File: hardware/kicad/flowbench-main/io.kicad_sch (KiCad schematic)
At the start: 57 parts, among them J18 Expander 2 spare, J19 Bleed stepper signals (GX16-8), J20 Bleed stepper 24 V (GX12-2), J21 Lift stepper signals (GX16-8), J22 Lift stepper 24 V (GX12-2), J23 Motor housing coils (GX16-8), J24 Motors-armed lamp, J25 E-stop (2 NC contacts), U11 TCA9535PWR #1 (0x20), U12 TCA9535PWR #2 (0x21), U13 TLP291-4, U14 TLP291-4, U15 TLP291-4, U16 AM26C31 (bleed stepper), U17 AM26C31 (lift stepper), U18 TBD62083AFWG, U19 74HCT123

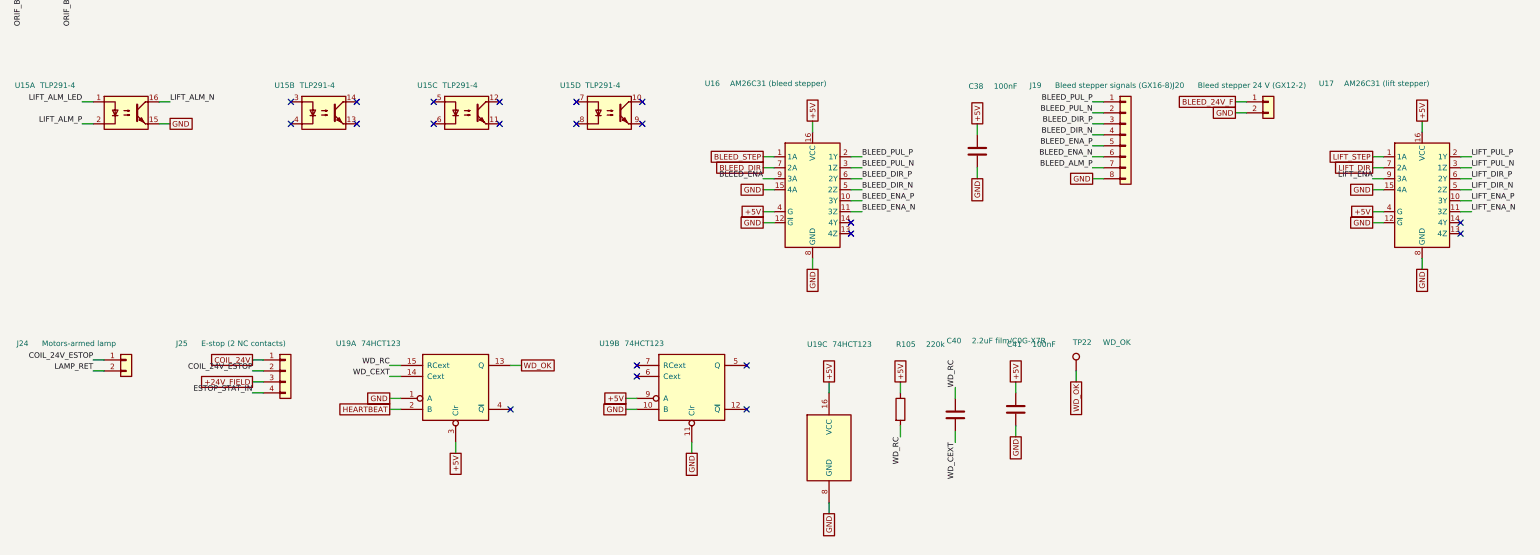
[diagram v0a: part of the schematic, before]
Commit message: KiCad: fix off-grid pins on ADS1219 and AM26C31 symbols
A floating-point modulo misread the symbol half-height as off-grid and
shifted it by half a step, leaving top and bottom pins 0.635 mm off the
1.27 mm connection grid (16 ERC warnings). verify.py now checks every pin
and wire end against the grid.

Co-Authored-By: Claude Opus 5.5 <noreply@anthropic.com>
Claude-Session: https://claude.ai/code/session_01QEmmugJA9S77dSDSNcKrPa
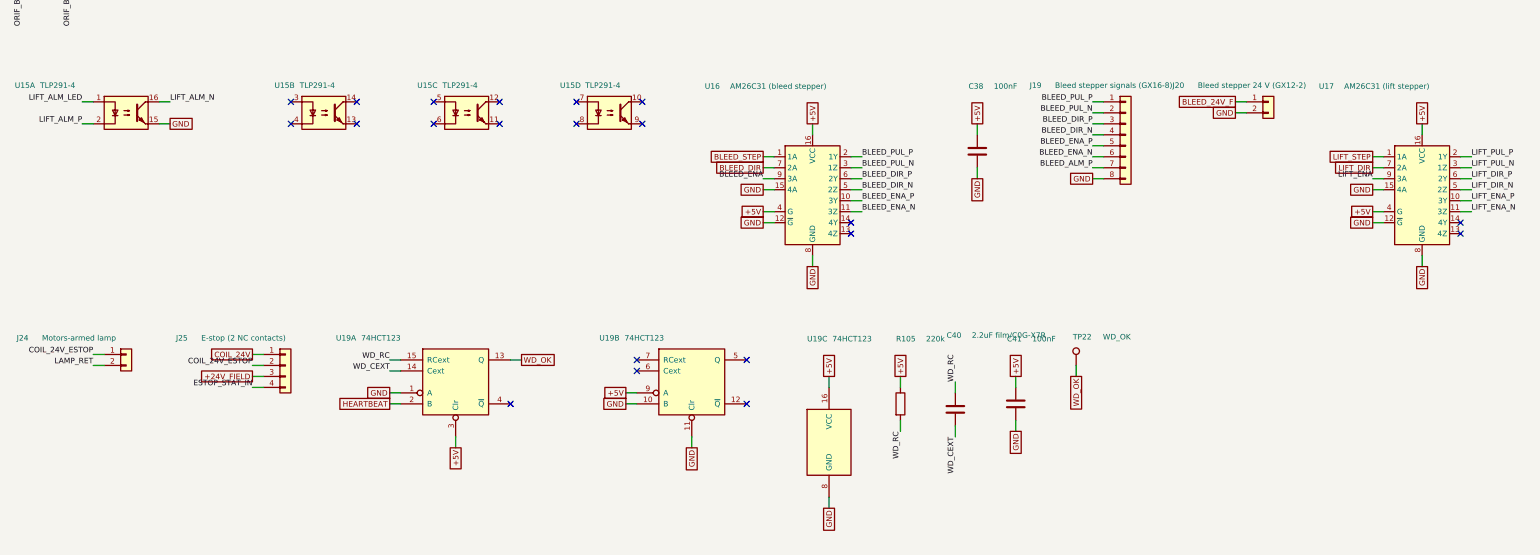
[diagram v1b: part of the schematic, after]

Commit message: KiCad: WIZ850io as one part with a two-row footprint
Pinout and size confirmed from the module (20 x 25 mm, two 1x6 headers).
The two header symbols become one 12-pin WIZ850io part on footprint
FlowBench:WIZ850io (J1 pads 1-6, J2 pads 7-12, rows 17.78 mm apart), so the
headers can't be placed at the wrong spacing.

Co-Authored-By: Claude Opus 5.5 <noreply@anthropic.com>
Claude-Session: https://claude.ai/code/session_01QEmmugJA9S77dSDSNcKrPa
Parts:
- removed J18: Expander 2 spare, Connector_PinHeader_2.54mm:PinHeader_1x10_P2.54mm_Vertical, symbol FlowBench:Conn_01x10
- removed J23: Motor housing coils (GX16-8), Connector_Phoenix_MC:PhoenixContact_MC_1,5_8-G-3.81_1x08_P3.81mm_Horizontal, symbol FlowBench:Conn_01x08
- removed J24: Motors-armed lamp, Connector_Phoenix_MC:PhoenixContact_MC_1,5_2-G-3.81_1x02_P3.81mm_Horizontal, symbol FlowBench:Conn_01x02
- removed J25: E-stop (2 NC contacts), Connector_Phoenix_MC:PhoenixContact_MC_1,5_4-G-3.81_1x04_P3.81mm_Horizontal, symbol FlowBench:Conn_01x04
- removed U11: TCA9535PWR #1 (0x20), Package_SO:TSSOP-24_4.4x7.8mm_P0.65mm, symbol FlowBench:TCA9535PWR
- removed U13: TLP291-4, Package_SO:SOIC-16_4.55x10.3mm_P1.27mm, symbol FlowBench:TLP291-4
- removed U16: AM26C31 (bleed stepper), Package_SO:SOIC-16_3.9x9.9mm_P1.27mm, symbol FlowBench:AM26C31
- removed U18: TBD62083AFWG, Package_SO:SOIC-18W_7.5x11.6mm_P1.27mm, symbol FlowBench:TBD62083AFWG
- removed U19: 74HCT123, Package_SO:SOIC-16_3.9x9.9mm_P1.27mm, symbol FlowBench:74HCT123
- added J16: Expander 2 spare, Connector_PinHeader_2.54mm:PinHeader_1x10_P2.54mm_Vertical, symbol FlowBench:Conn_01x10
- added J17: Bleed stepper signals (GX16-8), Connector_Phoenix_MC:PhoenixContact_MC_1,5_8-G-3.81_1x08_P3.81mm_Horizontal, symbol FlowBench:Conn_01x08
- added J18: Bleed stepper 24 V (GX12-2), Connector_Phoenix_MSTB:PhoenixContact_MSTBA_2,5_2-G-5,08_1x02_P5.08mm_Horizontal, symbol FlowBench:Conn_01x02
- added J23: E-stop (2 NC contacts), Connector_Phoenix_MC:PhoenixContact_MC_1,5_4-G-3.81_1x04_P3.81mm_Horizontal, symbol FlowBench:Conn_01x04
- added U13: TCA9535PWR #2 (0x21), Package_SO:TSSOP-24_4.4x7.8mm_P0.65mm, symbol FlowBench:TCA9535PWR
- added U16: TLP291-4, Package_SO:SOIC-16_4.55x10.3mm_P1.27mm, symbol FlowBench:TLP291-4
- added U18: AM26C31 (lift stepper), Package_SO:SOIC-16_3.9x9.9mm_P1.27mm, symbol FlowBench:AM26C31
- added U19: TBD62083AFWG, Package_SO:SOIC-18W_7.5x11.6mm_P1.27mm, symbol FlowBench:TBD62083AFWG
- added U20: 74HCT123, Package_SO:SOIC-16_3.9x9.9mm_P1.27mm, symbol FlowBench:74HCT123
- J19: value Bleed stepper signals (GX16-8) -> Lift stepper signals (GX16-8)
- J20: value Bleed stepper 24 V (GX12-2) -> Lift stepper 24 V (GX12-2)
- J21: value Lift stepper signals (GX16-8) -> Motor housing coils (GX16-8)
- J22: value Lift stepper 24 V (GX12-2) -> Motors-armed lamp; footprint Connector_Phoenix_MSTB:PhoenixContact_MSTBA_2,5_2-G-5,08_1x02_P5.08mm_Horizontal -> Connector_Phoenix_MC:PhoenixContact_MC_1,5_2-G-3.81_1x02_P3.81mm_Horizontal
- U12: value TCA9535PWR #2 (0x21) -> TCA9535PWR #1 (0x20)
- U17: value AM26C31 (lift stepper) -> AM26C31 (bleed stepper)
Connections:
- net +24V_FIELD: now also J23.3 (Pin_3)
- net +3V3: now also J16.9 (Pin_9), U13.21 (A0), U13.24 (VCC); no longer U12.21 (A0)
- net +5V: now also U18.16 (VCC), U18.4 (G), U20.16 (VCC), U20.3 (Clr), U20.9 (A)
- net BLEED_24V_F: now also J18.1 (Pin_1); no longer J20.1 (Pin_1)
- net BLEED_ALM_LED: now also U15.7; no longer U14.7
- net BLEED_ALM_N: now also U15.10, U13.9 (P05); no longer U12.9 (P05), U14.10
- net BLEED_ALM_P: now also U15.8, J17.7 (Pin_7); no longer J19.7 (Pin_7), U14.8
- net BLEED_DIR: now also U17.7 (2A)
- net BLEED_DIR_N: now also U17.5 (2Z), J17.4 (Pin_4); no longer J19.4 (Pin_4)
- net BLEED_DIR_P: now also U17.6 (2Y), J17.3 (Pin_3); no longer J19.3 (Pin_3)
- net BLEED_ENA: now also U12.13 (P10), U17.9 (3A)
- net BLEED_ENA_N: now also U17.11 (3Z), J17.6 (Pin_6); no longer J19.6 (Pin_6)
- net BLEED_ENA_P: now also U17.10 (3Y), J17.5 (Pin_5); no longer J19.5 (Pin_5)
- net BLEED_HOME_IN_LED: now also U14.3
- net BLEED_HOME_N: now also U12.16 (P13), U14.14
- net BLEED_PUL_N: now also U17.3 (1Z), J17.2 (Pin_2); no longer J19.2 (Pin_2)
- net BLEED_PUL_P: now also U17.2 (1Y), J17.1 (Pin_1); no longer J19.1 (Pin_1)
- net BLEED_PWR_EN: now also U12.11 (P07)
- net BLEED_STEP: now also U17.1 (1A)
- net COIL1_CMD: now also U12.4 (P00), U19.1 (I1)
- net COIL1_RET: now also J21.2 (Pin_2), U19.18 (O1)
- net COIL2_CMD: now also U12.5 (P01), U19.2 (I2)
- net COIL2_RET: now also J21.3 (Pin_3), U19.17 (O2)
- net COIL3_CMD: now also U12.6 (P02), U19.3 (I3)
- net COIL3_RET: now also J21.4 (Pin_4), U19.16 (O3)
- net COIL4_CMD: now also U12.7 (P03), U19.4 (I4)
- net COIL4_RET: now also J21.5 (Pin_5), U19.15 (O4)
- net COIL5_CMD: now also U12.8 (P04), U19.5 (I5)
- net COIL5_RET: now also J21.6 (Pin_6), U19.14 (O5)
- net COIL6_CMD: now also U12.9 (P05), U19.6 (I6)
- net COIL6_RET: now also J21.7 (Pin_7), U19.13 (O6)
- net COIL_24V: now also J23.1 (Pin_1)
- net COIL_24V_ESTOP: now also J21.1 (Pin_1), J22.1 (Pin_1), J23.2 (Pin_2), U19.10 (COM)
- net EFUSE_FLT_N: now also U13.11 (P07); no longer U12.11 (P07)
- net ESTOP_OK_N: now also U12.15 (P12), U14.16
- net ESTOP_STAT_IN: now also J23.4 (Pin_4)
- net ESTOP_STAT_IN_LED: now also U14.1
- net ETH_INT_EXP: now also U13.10 (P06); no longer U12.10 (P06)
- net ETH_RST_N: now also U12.14 (P11)
- net EXP2_P10: now also J16.1 (Pin_1), U13.13 (P10); no longer U12.13 (P10)
- net EXP2_P11: now also J16.2 (Pin_2), U13.14 (P11); no longer U12.14 (P11)
- net EXP2_P12: now also J16.3 (Pin_3), U13.15 (P12); no longer U12.15 (P12)
- net EXP2_P13: now also J16.4 (Pin_4), U13.16 (P13); no longer U12.16 (P13)
- net EXP2_P14: now also J16.5 (Pin_5), U13.17 (P14); no longer U12.17 (P14)
- net EXP2_P15: now also J16.6 (Pin_6), U13.18 (P15); no longer U12.18 (P15)
- net EXP2_P16: now also J16.7 (Pin_7), U13.19 (P16); no longer U12.19 (P16)
- net EXP2_P17: now also J16.8 (Pin_8), U13.20 (P17); no longer U12.20 (P17)
- net EXP_INT_N: now also U13.1 (~{INT})
- net GND: now also U12.21 (A0), U14.8, U15.11, U15.13, U15.2, U15.4, U15.6, U15.9, J16.10 (Pin_10), J17.8 (Pin_8), J18.2 (Pin_2), U13.12 (GND), U13.2 (A1), U13.3 (A2), U16.15, U18.12 (~{G}), U18.15 (4A), U18.8 (GND), U19.8 (I8), U19.9 (GND), U20.1 (A), U20.10 (B), U20.11 (Clr), U20.8 (GND); no longer J21.8 (Pin_8), J22.2 (Pin_2)
- net HEARTBEAT: now also U20.2 (B)
- net LAMP_CMD: now also U12.10 (P06), U19.7 (I7)
- net LAMP_RET: now also J22.2 (Pin_2), U19.12 (O7)
- net LIFT_24V_F: now also J20.1 (Pin_1); no longer J22.1 (Pin_1)
- net LIFT_ALM_LED: now also U16.1; no longer U15.1
- net LIFT_ALM_N: now also U13.6 (P02), U16.16; no longer U12.6 (P02), U15.16
- net LIFT_ALM_P: now also J19.7 (Pin_7), U16.2; no longer J21.7 (Pin_7), U15.2
- net LIFT_DIR: now also U18.7 (2A); no longer U17.7 (2A)
- net LIFT_DIR_N: now also J19.4 (Pin_4), U18.5 (2Z); no longer J21.4 (Pin_4), U17.5 (2Z)
- net LIFT_DIR_P: now also J19.3 (Pin_3), U18.6 (2Y); no longer J21.3 (Pin_3), U17.6 (2Y)
- net LIFT_ENA: now also U13.5 (P01), U18.9 (3A); no longer U12.5 (P01), U17.9 (3A)
- net LIFT_ENA_N: now also J19.6 (Pin_6), U18.11 (3Z); no longer J21.6 (Pin_6), U17.11 (3Z)
- net LIFT_ENA_P: now also J19.5 (Pin_5), U18.10 (3Y); no longer J21.5 (Pin_5), U17.10 (3Y)
- net LIFT_HOME_IN_LED: now also U14.5
- net LIFT_HOME_N: now also U14.12, U13.7 (P03); no longer U12.7 (P03)
- net LIFT_MAX_IN_LED: now also U14.7
- net LIFT_MAX_N: now also U14.10, U13.8 (P04); no longer U12.8 (P04)
- net LIFT_PUL_N: now also J19.2 (Pin_2), U18.3 (1Z); no longer J21.2 (Pin_2), U17.3 (1Z)
- net LIFT_PUL_P: now also J19.1 (Pin_1), U18.2 (1Y); no longer J21.1 (Pin_1), U17.2 (1Y)
- net LIFT_PWR_EN: now also U13.4 (P00); no longer U12.4 (P00)
- net LIFT_STEP: now also U18.1 (1A); no longer U17.1 (1A)
- net ORIF_B0_IN_LED: now also U15.1; no longer U14.1
- net ORIF_B0_N: now also U12.17 (P14), U15.16; no longer U14.16
- net ORIF_B1_IN_LED: now also U15.3; no longer U14.3
- net ORIF_B1_N: now also U12.18 (P15), U15.14; no longer U14.14
- net ORIF_B2_IN_LED: now also U15.5; no longer U14.5
- net ORIF_B2_N: now also U12.19 (P16), U15.12; no longer U14.12
- net SCL: now also U13.22 (SCL)
- net SDA: now also U13.23 (SDA)
- net SD_CD_N: now also U12.20 (P17)
- net WD_CEXT: now also U20.14 (Cext)
- net WD_OK: now also U20.13 (Q)
- net WD_RC: now also U20.15 (RCext)

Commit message: KiCad: DevKit as one part with a 25.4 mm two-row footprint
Header pinout confirmed against Espressif's J1/J3 tables; row spacing measured
at 25.4 mm. The two header symbols become one 44-pin ESP32-S3-DevKitC-1 part on
footprint FlowBench:ESP32-S3-DevKitC-1 (J1 pads 1-22, J3 pads 23-44), with the
antenna end marked. BOM notes the N32R16V as a drop-in alternative.

Co-Authored-By: Claude Opus 5.5 <noreply@anthropic.com>
Claude-Session: https://claude.ai/code/session_01QEmmugJA9S77dSDSNcKrPa
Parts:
- removed J16: Expander 2 spare, Connector_PinHeader_2.54mm:PinHeader_1x10_P2.54mm_Vertical, symbol FlowBench:Conn_01x10
- removed J21: Motor housing coils (GX16-8), Connector_Phoenix_MC:PhoenixContact_MC_1,5_8-G-3.81_1x08_P3.81mm_Horizontal, symbol FlowBench:Conn_01x08
- removed J22: Motors-armed lamp, Connector_Phoenix_MC:PhoenixContact_MC_1,5_2-G-3.81_1x02_P3.81mm_Horizontal, symbol FlowBench:Conn_01x02
- removed J23: E-stop (2 NC contacts), Connector_Phoenix_MC:PhoenixContact_MC_1,5_4-G-3.81_1x04_P3.81mm_Horizontal, symbol FlowBench:Conn_01x04
- removed U12: TCA9535PWR #1 (0x20), Package_SO:TSSOP-24_4.4x7.8mm_P0.65mm, symbol FlowBench:TCA9535PWR
- removed U14: TLP291-4, Package_SO:SOIC-16_4.55x10.3mm_P1.27mm, symbol FlowBench:TLP291-4
- removed U17: AM26C31 (bleed stepper), Package_SO:SOIC-16_3.9x9.9mm_P1.27mm, symbol FlowBench:AM26C31
- removed U19: TBD62083AFWG, Package_SO:SOIC-18W_7.5x11.6mm_P1.27mm, symbol FlowBench:TBD62083AFWG
- removed U20: 74HCT123, Package_SO:SOIC-16_3.9x9.9mm_P1.27mm, symbol FlowBench:74HCT123
- added J14: Expander 2 spare, Connector_PinHeader_2.54mm:PinHeader_1x10_P2.54mm_Vertical, symbol FlowBench:Conn_01x10
- added J15: Bleed stepper signals (GX16-8), Connector_Phoenix_MC:PhoenixContact_MC_1,5_8-G-3.81_1x08_P3.81mm_Horizontal, symbol FlowBench:Conn_01x08
- added J16: Bleed stepper 24 V (GX12-2), Connector_Phoenix_MSTB:PhoenixContact_MSTBA_2,5_2-G-5,08_1x02_P5.08mm_Horizontal, symbol FlowBench:Conn_01x02
- added J21: E-stop (2 NC contacts), Connector_Phoenix_MC:PhoenixContact_MC_1,5_4-G-3.81_1x04_P3.81mm_Horizontal, symbol FlowBench:Conn_01x04
- added U14: TCA9535PWR #2 (0x21), Package_SO:TSSOP-24_4.4x7.8mm_P0.65mm, symbol FlowBench:TCA9535PWR
- added U17: TLP291-4, Package_SO:SOIC-16_4.55x10.3mm_P1.27mm, symbol FlowBench:TLP291-4
- added U19: AM26C31 (lift stepper), Package_SO:SOIC-16_3.9x9.9mm_P1.27mm, symbol FlowBench:AM26C31
- added U20: TBD62083AFWG, Package_SO:SOIC-18W_7.5x11.6mm_P1.27mm, symbol FlowBench:TBD62083AFWG
- added U21: 74HCT123, Package_SO:SOIC-16_3.9x9.9mm_P1.27mm, symbol FlowBench:74HCT123
- J17: value Bleed stepper signals (GX16-8) -> Lift stepper signals (GX16-8)
- J18: value Bleed stepper 24 V (GX12-2) -> Lift stepper 24 V (GX12-2)
- J19: value Lift stepper signals (GX16-8) -> Motor housing coils (GX16-8)
- J20: value Lift stepper 24 V (GX12-2) -> Motors-armed lamp; footprint Connector_Phoenix_MSTB:PhoenixContact_MSTBA_2,5_2-G-5,08_1x02_P5.08mm_Horizontal -> Connector_Phoenix_MC:PhoenixContact_MC_1,5_2-G-3.81_1x02_P3.81mm_Horizontal
- U13: value TCA9535PWR #2 (0x21) -> TCA9535PWR #1 (0x20)
- U18: value AM26C31 (lift stepper) -> AM26C31 (bleed stepper)
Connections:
- net +24V_FIELD: now also J21.3 (Pin_3)
- net +3V3: now also J14.9 (Pin_9), U14.21 (A0), U14.24 (VCC); no longer U13.21 (A0)
- net +5V: now also U19.16 (VCC), U19.4 (G), U21.16 (VCC), U21.3 (Clr), U21.9 (A)
- net BLEED_24V_F: now also J16.1 (Pin_1); no longer J18.1 (Pin_1)
- net BLEED_ALM_LED: now also U16.7; no longer U15.7
- net BLEED_ALM_N: now also U16.10, U14.9 (P05); no longer U13.9 (P05), U15.10
- net BLEED_ALM_P: now also U16.8, J15.7 (Pin_7); no longer J17.7 (Pin_7), U15.8
- net BLEED_DIR: now also U18.7 (2A)
- net BLEED_DIR_N: now also U18.5 (2Z), J15.4 (Pin_4); no longer J17.4 (Pin_4)
- net BLEED_DIR_P: now also U18.6 (2Y), J15.3 (Pin_3); no longer J17.3 (Pin_3)
- net BLEED_ENA: now also U13.13 (P10), U18.9 (3A)
- net BLEED_ENA_N: now also U18.11 (3Z), J15.6 (Pin_6); no longer J17.6 (Pin_6)
- net BLEED_ENA_P: now also U18.10 (3Y), J15.5 (Pin_5); no longer J17.5 (Pin_5)
- net BLEED_HOME_IN_LED: now also U15.3
- net BLEED_HOME_N: now also U13.16 (P13), U15.14
- net BLEED_PUL_N: now also U18.3 (1Z), J15.2 (Pin_2); no longer J17.2 (Pin_2)
- net BLEED_PUL_P: now also U18.2 (1Y), J15.1 (Pin_1); no longer J17.1 (Pin_1)
- net BLEED_PWR_EN: now also U13.11 (P07)
- net BLEED_STEP: now also U18.1 (1A)
- net COIL1_CMD: now also U13.4 (P00), U20.1 (I1)
- net COIL1_RET: now also J19.2 (Pin_2), U20.18 (O1)
- net COIL2_CMD: now also U13.5 (P01), U20.2 (I2)
- net COIL2_RET: now also J19.3 (Pin_3), U20.17 (O2)
- net COIL3_CMD: now also U13.6 (P02), U20.3 (I3)
- net COIL3_RET: now also J19.4 (Pin_4), U20.16 (O3)
- net COIL4_CMD: now also U13.7 (P03), U20.4 (I4)
- net COIL4_RET: now also J19.5 (Pin_5), U20.15 (O4)
- net COIL5_CMD: now also U13.8 (P04), U20.5 (I5)
- net COIL5_RET: now also J19.6 (Pin_6), U20.14 (O5)
- net COIL6_CMD: now also U13.9 (P05), U20.6 (I6)
- net COIL6_RET: now also J19.7 (Pin_7), U20.13 (O6)
- net COIL_24V: now also J21.1 (Pin_1)
- net COIL_24V_ESTOP: now also J19.1 (Pin_1), J20.1 (Pin_1), J21.2 (Pin_2), U20.10 (COM)
- net EFUSE_FLT_N: now also U14.11 (P07); no longer U13.11 (P07)
- net ESTOP_OK_N: now also U13.15 (P12), U15.16
- net ESTOP_STAT_IN: now also J21.4 (Pin_4)
- net ESTOP_STAT_IN_LED: now also U15.1
- net ETH_INT_EXP: now also U14.10 (P06); no longer U13.10 (P06)
- net ETH_RST_N: now also U13.14 (P11)
- net EXP2_P10: now also J14.1 (Pin_1), U14.13 (P10); no longer U13.13 (P10)
- net EXP2_P11: now also J14.2 (Pin_2), U14.14 (P11); no longer U13.14 (P11)
- net EXP2_P12: now also J14.3 (Pin_3), U14.15 (P12); no longer U13.15 (P12)
- net EXP2_P13: now also J14.4 (Pin_4), U14.16 (P13); no longer U13.16 (P13)
- net EXP2_P14: now also J14.5 (Pin_5), U14.17 (P14); no longer U13.17 (P14)
- net EXP2_P15: now also J14.6 (Pin_6), U14.18 (P15); no longer U13.18 (P15)
- net EXP2_P16: now also J14.7 (Pin_7), U14.19 (P16); no longer U13.19 (P16)
- net EXP2_P17: now also J14.8 (Pin_8), U14.20 (P17); no longer U13.20 (P17)
- net EXP_INT_N: now also U14.1 (~{INT})
- net GND: now also U13.21 (A0), U15.8, U16.11, U16.13, U16.2, U16.4, U16.6, U16.9, J14.10 (Pin_10), J15.8 (Pin_8), J16.2 (Pin_2), U14.12 (GND), U14.2 (A1), U14.3 (A2), U17.15, U19.12 (~{G}), U19.15 (4A), U19.8 (GND), U20.8 (I8), U20.9 (GND), U21.1 (A), U21.10 (B), U21.11 (Clr), U21.8 (GND); no longer J19.8 (Pin_8), J20.2 (Pin_2)
- net HEARTBEAT: now also U21.2 (B)
- net LAMP_CMD: now also U13.10 (P06), U20.7 (I7)
- net LAMP_RET: now also J20.2 (Pin_2), U20.12 (O7)
- net LIFT_24V_F: now also J18.1 (Pin_1); no longer J20.1 (Pin_1)
- net LIFT_ALM_LED: now also U17.1; no longer U16.1
- net LIFT_ALM_N: now also U14.6 (P02), U17.16; no longer U13.6 (P02), U16.16
- net LIFT_ALM_P: now also J17.7 (Pin_7), U17.2; no longer J19.7 (Pin_7), U16.2
- net LIFT_DIR: now also U19.7 (2A); no longer U18.7 (2A)
- net LIFT_DIR_N: now also J17.4 (Pin_4), U19.5 (2Z); no longer J19.4 (Pin_4), U18.5 (2Z)
- net LIFT_DIR_P: now also J17.3 (Pin_3), U19.6 (2Y); no longer J19.3 (Pin_3), U18.6 (2Y)
- net LIFT_ENA: now also U14.5 (P01), U19.9 (3A); no longer U13.5 (P01), U18.9 (3A)
- net LIFT_ENA_N: now also J17.6 (Pin_6), U19.11 (3Z); no longer J19.6 (Pin_6), U18.11 (3Z)
- net LIFT_ENA_P: now also J17.5 (Pin_5), U19.10 (3Y); no longer J19.5 (Pin_5), U18.10 (3Y)
- net LIFT_HOME_IN_LED: now also U15.5
- net LIFT_HOME_N: now also U15.12, U14.7 (P03); no longer U13.7 (P03)
- net LIFT_MAX_IN_LED: now also U15.7
- net LIFT_MAX_N: now also U15.10, U14.8 (P04); no longer U13.8 (P04)
- net LIFT_PUL_N: now also J17.2 (Pin_2), U19.3 (1Z); no longer J19.2 (Pin_2), U18.3 (1Z)
- net LIFT_PUL_P: now also J17.1 (Pin_1), U19.2 (1Y); no longer J19.1 (Pin_1), U18.2 (1Y)
- net LIFT_PWR_EN: now also U14.4 (P00); no longer U13.4 (P00)
- net LIFT_STEP: now also U19.1 (1A); no longer U18.1 (1A)
- net ORIF_B0_IN_LED: now also U16.1; no longer U15.1
- net ORIF_B0_N: now also U13.17 (P14), U16.16; no longer U15.16
- net ORIF_B1_IN_LED: now also U16.3; no longer U15.3
- net ORIF_B1_N: now also U13.18 (P15), U16.14; no longer U15.14
- net ORIF_B2_IN_LED: now also U16.5; no longer U15.5
- net ORIF_B2_N: now also U13.19 (P16), U16.12; no longer U15.12
- net SCL: now also U14.22 (SCL)
- net SDA: now also U14.23 (SDA)
- net SD_CD_N: now also U13.20 (P17)
- net WD_CEXT: now also U21.14 (Cext)
- net WD_OK: now also U21.13 (Q)
- net WD_RC: now also U21.15 (RCext)
